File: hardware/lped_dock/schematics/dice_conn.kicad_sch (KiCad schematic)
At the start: 5 parts, among them J2 V_{OUT}, J3 BUTTON, J4 CONN, J5 LED, J6 GND

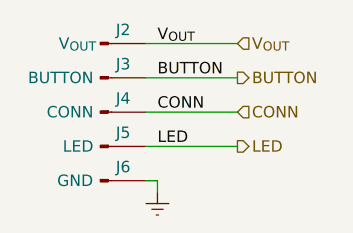
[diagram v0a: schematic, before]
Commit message: feat(hardware): remove unused parts from dock pcb
* Removed LED from dock
* Removed button from dock
* Removed connection pins for LED and button
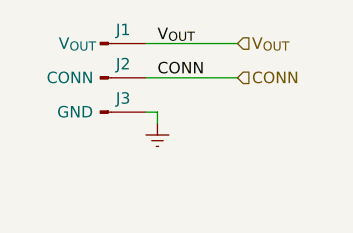
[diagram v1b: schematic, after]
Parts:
- removed J3: BUTTON, Connector_Pin:Pin_D0.9mm_L10.0mm_W2.4mm_FlatFork, symbol Connector:Conn_01x01_Pin
- removed J5: LED, Connector_Pin:Pin_D0.9mm_L10.0mm_W2.4mm_FlatFork, symbol Connector:Conn_01x01_Pin
- renumbered J2 to J1, J4 to J2, J6 to J3
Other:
- moved on the sheet: J2, J3
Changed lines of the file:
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@@
 	(wire
 		(pts
-			(xy 133.35 99.06) (xy 134.62 99.06)
+			(xy 133.35 91.44) (xy 134.62 91.44)
 		)
 		(stroke
@@
 	(wire
 		(pts
-			(xy 143.51 95.25) (xy 133.35 95.25)
+			(xy 143.51 87.63) (xy 133.35 87.63)
 		)
 		(stroke
@@
 	(wire
 		(pts
-			(xy 143.51 91.44) (xy 133.35 91.44)
+			(xy 133.35 83.82) (xy 143.51 83.82)
 		)
 		(stroke
@@
 	(wire
 		(pts
-			(xy 133.35 83.82) (xy 143.51 83.82)
+			(xy 134.62 91.44) (xy 134.62 92.71)
 		)
 		(stroke
@@
 		)
 	)
-	(wire
-		(pts
-			(xy 134.62 99.06) (xy 134.62 100.33)
-		)
-		(stroke
-			(width 0)
-			(type default)
-		)
-	)
-	(wire
-		(pts
-			(xy 143.51 87.63) (xy 133.35 87.63)
-		)
-		(stroke
-			(width 0)
-			(type default)
-		)
-	)
 	(label "CONN"
-		(at 134.62 91.44 0)
-		(effects
-			(font
-				(size 1.27 1.27)
-			)
-			(justify left bottom)
-		)
-	)
-	(label "BUTTON"
 		(at 134.62 87.63 0)
 		(effects
@@
 			)
 			(justify left bottom)
-		)
-	)
-	(label "LED"
-		(at 134.62 95.25 0)
-		(effects
-			(font
-				(size 1.27 1.27)
-			)
-			(justify left bottom)
-		)
-	)
-	(hierarchical_label "LED"
-		(shape output)
-		(at 143.51 95.25 0)
-		(effects
-			(font
-				(size 1.27 1.27)
-			)
-			(justify left)
-		)
-	)
-	(hierarchical_label "BUTTON"
-		(shape output)
-		(at 143.51 87.63 0)
-		(effects
-			(font
-				(size 1.27 1.27)
-			)
-			(justify left)
 		)
 	)
@@
 	(hierarchical_label "CONN"
 		(shape input)
-		(at 143.51 91.44 0)
+		(at 143.51 87.63 0)
 		(effects
 			(font
@@
 		(on_board yes)
 		(dnp no)
-		(property "Reference" "J3"
+		(property "Reference" "J2"
 			(at 130.81 86.106 0)
 			(effects
@@
 			)
 		)
-		(property "Value" "BUTTON"
+		(property "Value" "CONN"
 			(at 127.508 87.63 0)
 			(effects
@@
 			(project "lped_dock"
 				(path "/5c78e66f-0328-4fd7-bcaa-ded4a2671f1d/8c8f9994-8fdf-4504-abf2-e4b10712cebd"
-					(reference "J3")
+					(reference "J2")
+					(unit 1)
+				)
+			)
+		)
+	)
+	(symbol
+		(lib_id "Connector:Conn_01x01_Pin")
+		(at 128.27 83.82 0)
+		(unit 1)
+		(exclude_from_sim no)
+		(in_bom yes)
+		(on_board yes)
+		(dnp no)
+		(property "Reference" "J1"
+			(at 130.81 82.296 0)
+			(effects
+				(font
+					(size 1.27 1.27)
+				)
+			)
+		)
+		(property "Value" "V_{OUT}"
+			(at 125.73 83.82 0)
+			(effects
+				(font
+					(size 1.27 1.27)
+				)
+			)
+		)
+		(property "Footprint" "Connector_Pin:Pin_D0.9mm_L10.0mm_W2.4mm_FlatFork"
+			(at 128.27 83.82 0)
+			(effects
+				(font
+					(size 1.27 1.27)
+				)
+				(hide yes)
+			)
+		)
+		(property "Datasheet" "~"
+			(at 128.27 83.82 0)
+			(effects
+				(font
+					(size 1.27 1.27)
+				)
+				(hide yes)
+			)
+		)
+		(property "Description" "Generic connector, single row, 01x01, script generated"
+			(at 128.27 83.82 0)
+			(effects
+				(font
+					(size 1.27 1.27)
+				)
+				(hide yes)
+			)
+		)
+		(pin "1"
+		)
+		(instances
+			(project "lped_dock"
+				(path "/5c78e66f-0328-4fd7-bcaa-ded4a2671f1d/8c8f9994-8fdf-4504-abf2-e4b10712cebd"
+					(reference "J1")
 					(unit 1)
 				)
@@
 		(on_board yes)
 		(dnp no)
-		(property "Reference" "J4"
+		(property "Reference" "J3"
 			(at 130.81 89.916 0)
 			(effects
@@
 			)
 		)
-		(property "Value" "CONN"
-			(at 127.508 91.44 0)
-			(effects
-				(font
-					(size 1.27 1.27)
-				)
-				(justify right)
+		(property "Value" "GND"
+			(at 125.476 91.44 0)
+			(effects
+				(font
+					(size 1.27 1.27)
+				)
 			)
 		)
@@
 			(project "lped_dock"
 				(path "/5c78e66f-0328-4fd7-bcaa-ded4a2671f1d/8c8f9994-8fdf-4504-abf2-e4b10712cebd"
-					(reference "J4")
-					(unit 1)
-				)
-			)
-		)
-	)
-	(symbol
-		(lib_id "Connector:Conn_01x01_Pin")
-		(at 128.27 95.25 0)
-		(unit 1)
-		(exclude_from_sim no)
-		(in_bom yes)
-		(on_board yes)
-		(dnp no)
-		(property "Reference" "J5"
-			(at 130.81 93.726 0)
-			(effects
-				(font
-					(size 1.27 1.27)
-				)
-			)
-		)
-		(property "Value" "LED"
-			(at 127.508 95.25 0)
-			(effects
-				(font
-					(size 1.27 1.27)
-				)
-				(justify right)
-			)
-		)
-		(property "Footprint" "Connector_Pin:Pin_D0.9mm_L10.0mm_W2.4mm_FlatFork"
-			(at 128.27 95.25 0)
-			(effects
-				(font
-					(size 1.27 1.27)
-				)
-				(hide yes)
-			)
-		)
-		(property "Datasheet" "~"
-			(at 128.27 95.25 0)
-			(effects
-				(font
-					(size 1.27 1.27)
-				)
-				(hide yes)
-			)
-		)
-		(property "Description" "Generic connector, single row, 01x01, script generated"
-			(at 128.27 95.25 0)
-			(effects
-				(font
-					(size 1.27 1.27)
-				)
-				(hide yes)
-			)
-		)
-		(pin "1"
-		)
-		(instances
-			(project "lped_dock"
-				(path "/5c78e66f-0328-4fd7-bcaa-ded4a2671f1d/8c8f9994-8fdf-4504-abf2-e4b10712cebd"
-					(reference "J5")
-					(unit 1)
-				)
-			)
-		)
-	)
-	(symbol
-		(lib_id "Connector:Conn_01x01_Pin")
-		(at 128.27 83.82 0)
-		(unit 1)
-		(exclude_from_sim no)
-		(in_bom yes)
-		(on_board yes)
-		(dnp no)
-		(property "Reference" "J2"
-			(at 130.81 82.296 0)
-			(effects
-				(font
-					(size 1.27 1.27)
-				)
-			)
-		)
-		(property "Value" "V_{OUT}"
-			(at 125.73 83.82 0)
-			(effects
-				(font
-					(size 1.27 1.27)
-				)
-			)
-		)
-		(property "Footprint" "Connector_Pin:Pin_D0.9mm_L10.0mm_W2.4mm_FlatFork"
-			(at 128.27 83.82 0)
-			(effects
-				(font
-					(size 1.27 1.27)
-				)
-				(hide yes)
-			)
-		)
-		(property "Datasheet" "~"
-			(at 128.27 83.82 0)
-			(effects
-				(font
-					(size 1.27 1.27)
-				)
-				(hide yes)
-			)
-		)
-		(property "Description" "Generic connector, single row, 01x01, script generated"
-			(at 128.27 83.82 0)
-			(effects
-				(font
-					(size 1.27 1.27)
-				)
-				(hide yes)
-			)
-		)
-		(pin "1"
-		)
-		(instances
-			(project "lped_dock"
-				(path "/5c78e66f-0328-4fd7-bcaa-ded4a2671f1d/8c8f9994-8fdf-4504-abf2-e4b10712cebd"
-					(reference "J2")
-					(unit 1)
-				)
-			)
-		)
-	)
-	(symbol
-		(lib_id "Connector:Conn_01x01_Pin")
-		(at 128.27 99.06 0)
-		(unit 1)
-		(exclude_from_sim no)
-		(in_bom yes)
-		(on_board yes)
-		(dnp no)
-		(property "Reference" "J6"
-			(at 130.81 97.536 0)
-			(effects
-				(font
-					(size 1.27 1.27)
-				)
-			)
-		)
-		(property "Value" "GND"
-			(at 125.476 99.06 0)
-			(effects
-				(font
-					(size 1.27 1.27)
-				)
-			)
-		)
-		(property "Footprint" "Connector_Pin:Pin_D0.9mm_L10.0mm_W2.4mm_FlatFork"
-			(at 128.27 99.06 0)
-			(effects
-				(font
-					(size 1.27 1.27)
-				)
-				(hide yes)
-			)
-		)
-		(property "Datasheet" "~"
-			(at 128.27 99.06 0)
-			(effects
-				(font
-					(size 1.27 1.27)
-				)
-				(hide yes)
-			)
-		)
-		(property "Description" "Generic connector, single row, 01x01, script generated"
-			(at 128.27 99.06 0)
-			(effects
-				(font
-					(size 1.27 1.27)
-				)
-				(hide yes)
-			)
-		)
-		(pin "1"
-		)
-		(instances
-			(project "lped_dock"
-				(path "/5c78e66f-0328-4fd7-bcaa-ded4a2671f1d/8c8f9994-8fdf-4504-abf2-e4b10712cebd"
-					(reference "J6")
+					(reference "J3")
 					(unit 1)
 				)
@@
 	(symbol
 		(lib_id "power:Earth")
-		(at 134.62 100.33 0)
+		(at 134.62 92.71 0)
 		(unit 1)
 		(exclude_from_sim no)
@@
 		(dnp no)
 		(fields_autoplaced yes)
-		(property "Reference" "#PWR02"
-			(at 134.62 106.68 0)
+		(property "Reference" "#PWR01"
+			(at 134.62 99.06 0)
 			(effects
 				(font
@@
 		)
 		(property "Value" "Earth"
-			(at 134.62 105.41 0)
+			(at 134.62 97.79 0)
 			(effects
 				(font
@@
 		)
 		(property "Footprint" ""
-			(at 134.62 100.33 0)
+			(at 134.62 92.71 0)
 			(effects
 				(font
@@
 		)
 		(property "Datasheet" "~"
-			(at 134.62 100.33 0)
+			(at 134.62 92.71 0)
 			(effects
 				(font
@@
 		)
 		(property "Description" "Power symbol creates a global label with name \"Earth\""
-			(at 134.62 100.33 0)
+			(at 134.62 92.71 0)
 			(effects
 				(font
@@
 			(project "lped_dock"
 				(path "/5c78e66f-0328-4fd7-bcaa-ded4a2671f1d/8c8f9994-8fdf-4504-abf2-e4b10712cebd"
-					(reference "#PWR02")
+					(reference "#PWR01")
 					(unit 1)
 				)
